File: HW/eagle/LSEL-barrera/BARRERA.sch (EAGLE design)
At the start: 8 parts

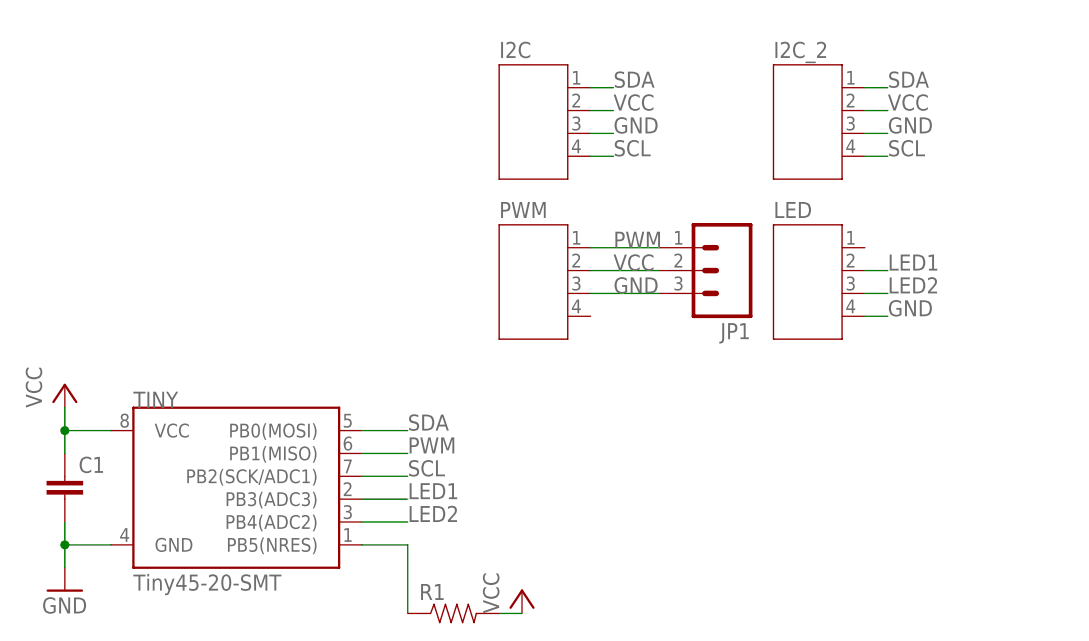
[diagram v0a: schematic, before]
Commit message: Barrera RJ changed
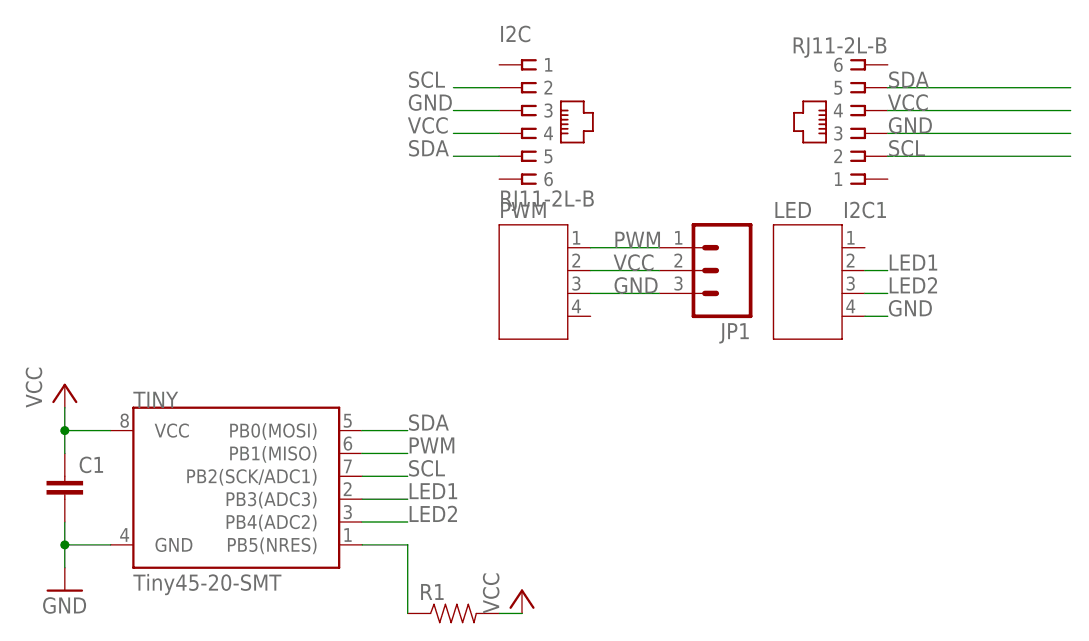
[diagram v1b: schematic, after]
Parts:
- removed I2C_2: (no value), jst-ph:JST-PH4
- added I2C1: RJ11-2L-B, con-tycoelectronics:RJ11-2L-B
- I2C: value (none) -> RJ11-2L-B; device jst-ph:JST-PH4 -> con-tycoelectronics:RJ11-2L-B
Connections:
- net GND: now also I2C1.3; no longer I2C_2.3
- net SCL: now also I2C.2, I2C1.2; no longer I2C.4, I2C_2.4
- net SDA: now also I2C.5, I2C1.5; no longer I2C.1, I2C_2.1
- net VCC: now also I2C.4, I2C1.4; no longer I2C.2, I2C_2.2
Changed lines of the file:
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@@
 <?xml version="1.0" encoding="utf-8"?>
 <!DOCTYPE eagle SYSTEM "eagle.dtd">
-<eagle version="6.3">
+<eagle version="7.2.0">
 <drawing>
 <settings>
@@
 <part name="C1" library="SparkFun-Capacitors" deviceset="CAP" device="0603-CAP"/>
 <part name="R1" library="SparkFun-Resistors" deviceset="RESISTOR" device="0603"/>
-<part name="I2C" library="jst-ph" deviceset="JST-PH4" device=""/>
-<part name="I2C_2" library="jst-ph" deviceset="JST-PH4" device=""/>
+<part name="I2C" library="con-tycoelectronics" deviceset="RJ11" device="" technology="-2L-B"/>
 <part name="PWM" library="jst-ph" deviceset="JST-PH4" device=""/>
 <part name="LED" library="jst-ph" deviceset="JST-PH4" device=""/>
@@
 <part name="P+2" library="supply1" deviceset="VCC" device=""/>
 <part name="JP1" library="SparkFun" deviceset="M03" device="PTH"/>
+<part name="I2C1" library="con-tycoelectronics" deviceset="RJ11" device="" technology="-2L-B"/>
 </parts>
 <sheets>
@@
 <instance part="C1" gate="G$1" x="40.64" y="48.26"/>
 <instance part="R1" gate="G$1" x="83.82" y="35.56"/>
-<instance part="I2C" gate="A" x="91.44" y="91.44"/>
-<instance part="I2C_2" gate="A" x="121.92" y="91.44"/>
+<instance part="I2C" gate="G$1" x="91.44" y="91.44"/>
 <instance part="PWM" gate="A" x="91.44" y="73.66"/>
 <instance part="LED" gate="A" x="121.92" y="73.66"/>
@@
 <instance part="P+2" gate="VCC" x="91.44" y="38.1"/>
 <instance part="JP1" gate="G$1" x="114.3" y="73.66" rot="R180"/>
+<instance part="I2C1" gate="G$1" x="129.54" y="88.9" rot="R180"/>
 </instances>
 <busses>
@@
 </segment>
 <segment>
-<pinref part="I2C" gate="A" pin="4"/>
-<wire x1="99.06" y1="86.36" x2="101.6" y2="86.36" width="0.1524" layer="91"/>
-<label x="101.6" y="86.36" size="1.778" layer="95"/>
-</segment>
-<segment>
-<pinref part="I2C_2" gate="A" pin="4"/>
-<wire x1="129.54" y1="86.36" x2="132.08" y2="86.36" width="0.1524" layer="91"/>
+<pinref part="I2C" gate="G$1" pin="2"/>
+<wire x1="88.9" y1="93.98" x2="83.82" y2="93.98" width="0.1524" layer="91"/>
+<label x="78.74" y="93.98" size="1.778" layer="95"/>
+</segment>
+<segment>
+<wire x1="152.4" y1="86.36" x2="132.08" y2="86.36" width="0.1524" layer="91"/>
 <label x="132.08" y="86.36" size="1.778" layer="95"/>
+<pinref part="I2C1" gate="G$1" pin="2"/>
 </segment>
 </net>
@@
 </segment>
 <segment>
-<pinref part="I2C" gate="A" pin="1"/>
-<wire x1="99.06" y1="93.98" x2="101.6" y2="93.98" width="0.1524" layer="91"/>
-<label x="101.6" y="93.98" size="1.778" layer="95"/>
-</segment>
-<segment>
-<pinref part="I2C_2" gate="A" pin="1"/>
-<wire x1="129.54" y1="93.98" x2="132.08" y2="93.98" width="0.1524" layer="91"/>
+<pinref part="I2C" gate="G$1" pin="5"/>
+<wire x1="88.9" y1="86.36" x2="83.82" y2="86.36" width="0.1524" layer="91"/>
+<label x="78.74" y="86.36" size="1.778" layer="95"/>
+</segment>
+<segment>
+<wire x1="152.4" y1="93.98" x2="132.08" y2="93.98" width="0.1524" layer="91"/>
 <label x="132.08" y="93.98" size="1.778" layer="95"/>
+<pinref part="I2C1" gate="G$1" pin="5"/>
 </segment>
 </net>
@@
 </segment>
 <segment>
-<pinref part="I2C" gate="A" pin="3"/>
-<wire x1="99.06" y1="88.9" x2="101.6" y2="88.9" width="0.1524" layer="91"/>
-<label x="101.6" y="88.9" size="1.778" layer="95"/>
-</segment>
-<segment>
-<pinref part="I2C_2" gate="A" pin="3"/>
-<wire x1="129.54" y1="88.9" x2="132.08" y2="88.9" width="0.1524" layer="91"/>
+<pinref part="I2C" gate="G$1" pin="3"/>
+<wire x1="88.9" y1="91.44" x2="83.82" y2="91.44" width="0.1524" layer="91"/>
+<label x="78.74" y="91.44" size="1.778" layer="95"/>
+</segment>
+<segment>
+<wire x1="152.4" y1="88.9" x2="132.08" y2="88.9" width="0.1524" layer="91"/>
 <label x="132.08" y="88.9" size="1.778" layer="95"/>
+<pinref part="I2C1" gate="G$1" pin="3"/>
 </segment>
 </net>
@@
 </segment>
 <segment>
-<pinref part="I2C" gate="A" pin="2"/>
-<wire x1="99.06" y1="91.44" x2="101.6" y2="91.44" width="0.1524" layer="91"/>
-<label x="101.6" y="91.44" size="1.778" layer="95"/>
-</segment>
-<segment>
-<pinref part="I2C_2" gate="A" pin="2"/>
-<wire x1="129.54" y1="91.44" x2="132.08" y2="91.44" width="0.1524" layer="91"/>
+<pinref part="I2C" gate="G$1" pin="4"/>
+<wire x1="88.9" y1="88.9" x2="83.82" y2="88.9" width="0.1524" layer="91"/>
+<label x="78.74" y="88.9" size="1.778" layer="95"/>
+</segment>
+<segment>
+<wire x1="152.4" y1="91.44" x2="132.08" y2="91.44" width="0.1524" layer="91"/>
 <label x="132.08" y="91.44" size="1.778" layer="95"/>
-</segment>
-</net>
+<pinref part="I2C1" gate="G$1" pin="4"/>
+</segment>
+</net>
